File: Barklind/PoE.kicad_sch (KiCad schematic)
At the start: 8 parts, among them U2 TPS2375-1

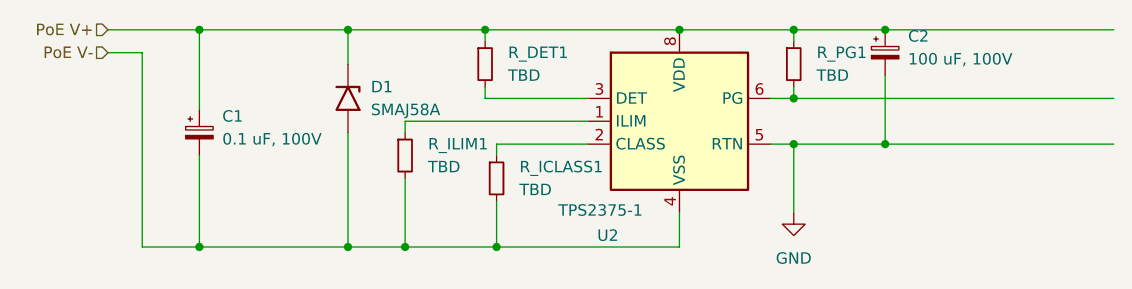
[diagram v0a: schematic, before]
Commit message: Added Ethercat schematic Added W5500 to component suggestions Added picture to explain CD4007UB wiring
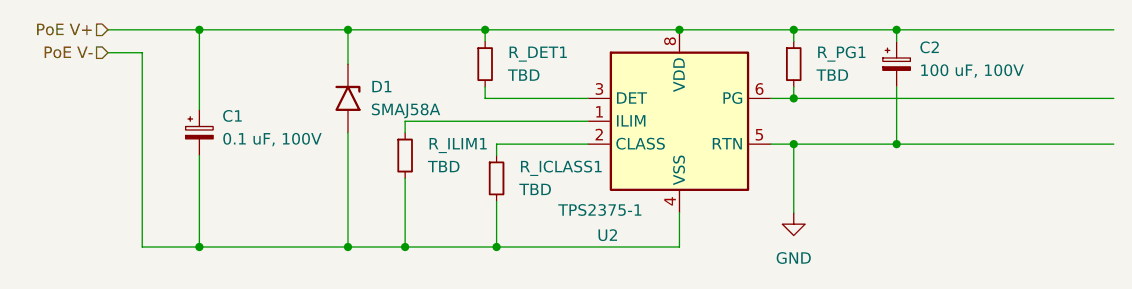
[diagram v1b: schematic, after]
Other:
- moved on the sheet: C2
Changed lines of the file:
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@@
-	)
-	(junction
-		(at 139.7 71.12)
-		(diameter 0)
-		(color 0 0 0 0)
 	)
 	(junction
@@
 	)
 	(junction
+		(at 140.97 83.82)
+		(diameter 0)
+		(color 0 0 0 0)
+	)
+	(junction
+		(at 140.97 71.12)
+		(diameter 0)
+		(color 0 0 0 0)
+	)
+	(junction
 		(at 129.54 83.82)
 		(diameter 0)
@@
 		(color 0 0 0 0)
 	)
-	(junction
-		(at 139.7 83.82)
-		(diameter 0)
-		(color 0 0 0 0)
-	)
 	(wire
 		(pts
@@
 	(wire
 		(pts
-			(xy 139.7 71.12) (xy 165.1 71.12)
-		)
-		(stroke
-			(width 0)
-			(type default)
-		)
-	)
-	(wire
-		(pts
 			(xy 86.36 81.28) (xy 106.68 81.28)
 		)
@@
 	(wire
 		(pts
-			(xy 139.7 76.2) (xy 139.7 83.82)
+			(xy 140.97 77.47) (xy 140.97 83.82)
 		)
 		(stroke
@@
 	(wire
 		(pts
-			(xy 139.7 83.82) (xy 165.1 83.82)
-		)
-		(stroke
-			(width 0)
-			(type default)
-		)
-	)
-	(wire
-		(pts
 			(xy 53.34 73.66) (xy 57.15 73.66)
 		)
@@
 	(wire
 		(pts
+			(xy 140.97 83.82) (xy 165.1 83.82)
+		)
+		(stroke
+			(width 0)
+			(type default)
+		)
+	)
+	(wire
+		(pts
 			(xy 63.5 85.09) (xy 63.5 95.25)
 		)
@@
 	(wire
 		(pts
+			(xy 140.97 71.12) (xy 165.1 71.12)
+		)
+		(stroke
+			(width 0)
+			(type default)
+		)
+	)
+	(wire
+		(pts
 			(xy 96.52 83.82) (xy 106.68 83.82)
 		)
@@
 	(wire
 		(pts
-			(xy 139.7 83.82) (xy 129.54 83.82)
+			(xy 129.54 83.82) (xy 140.97 83.82)
+		)
+		(stroke
+			(width 0)
+			(type default)
+		)
+	)
+	(wire
+		(pts
+			(xy 140.97 72.39) (xy 140.97 71.12)
 		)
 		(stroke
@@
 	(wire
 		(pts
-			(xy 129.54 71.12) (xy 139.7 71.12)
+			(xy 129.54 71.12) (xy 140.97 71.12)
 		)
 		(stroke
@@
 	(symbol
 		(lib_id "Device:C_Polarized_Small")
-		(at 139.7 73.66 0)
+		(at 140.97 74.93 0)
 		(unit 1)
 		(exclude_from_sim no)
@@
 		(fields_autoplaced yes)
 		(property "Reference" "C2"
-			(at 142.24 71.8438 0)
+			(at 143.51 73.1138 0)
 			(effects
 				(font
@@
 		)
 		(property "Value" "100 uF, 100V"
-			(at 142.24 74.3838 0)
+			(at 143.51 75.6538 0)
 			(effects
 				(font
@@
 		)
 		(property "Footprint" ""
-			(at 139.7 73.66 0)
+			(at 140.97 74.93 0)
 			(effects
 				(font
@@
 		)
 		(property "Datasheet" "~"
-			(at 139.7 73.66 0)
+			(at 140.97 74.93 0)
 			(effects
 				(font
@@
 		)
 		(property "Description" "Polarized capacitor, small symbol"
-			(at 139.7 73.66 0)
-			(effects
-				(font
+			(at 140.97 74.93 0)
+			(effects
+				(font

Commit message: Added basic board (with no layout specified) Added additional comments to schematic
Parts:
- R_DET1, R_ICLASS1, R_ILIM1, R_PG1: footprint (none) -> Resistor_SMD:R_0805_2012Metric
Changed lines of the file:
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@@
 			)
 		)
-		(property "Footprint" ""
+		(property "Footprint" "Resistor_SMD:R_0805_2012Metric"
 			(at 95.25 74.93 0)
 			(effects
@@
 			)
 		)
-		(property "Footprint" ""
+		(property "Footprint" "Resistor_SMD:R_0805_2012Metric"
 			(at 86.36 85.09 0)
 			(effects
@@
 			)
 		)
-		(property "Footprint" ""
+		(property "Footprint" "Resistor_SMD:R_0805_2012Metric"
 			(at 129.54 74.93 0)
 			(effects
@@
 			)
 		)
-		(property "Footprint" ""
+		(property "Footprint" "Resistor_SMD:R_0805_2012Metric"
 			(at 96.52 87.63 0)
 			(effects
